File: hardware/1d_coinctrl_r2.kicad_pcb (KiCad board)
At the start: 2 copper layers, 158.8 x 159.8 mm, 97 parts, among them J1 +12V INPUT, J10 USB_B, J2 CO LINE, J3 V_RLY_SEL, J5 COIN LINE, J6 DB9_Female_MountingHoles, J7 Conn_01x02, J8 Conn_02x10_Odd_Even, J9 Conn_01x06_Male, K1 G5V-2-DC12, K10 L4_COIN_CTRL, K11 G5V-2-DC12, K2 G5V-2-DC12, K3 L1_HOLD, K4 L1_COIN_CTRL, K5 L2_HOLD, K6 L2_COIN_CTRL, K7 L3_HOLD, K8 L3_COIN_CTRL, K9 L4_HOLD, SW1 SW_Push, U1 MCP23008-xP, U10 ILD74, U14 MAX202, U2 V7805-1000, U3 PIC18F4550-IP, U4 74LS06, U5 74LS06, U6 H11AA1, U7 ILD74, U8 ILD74, U9 ILD74

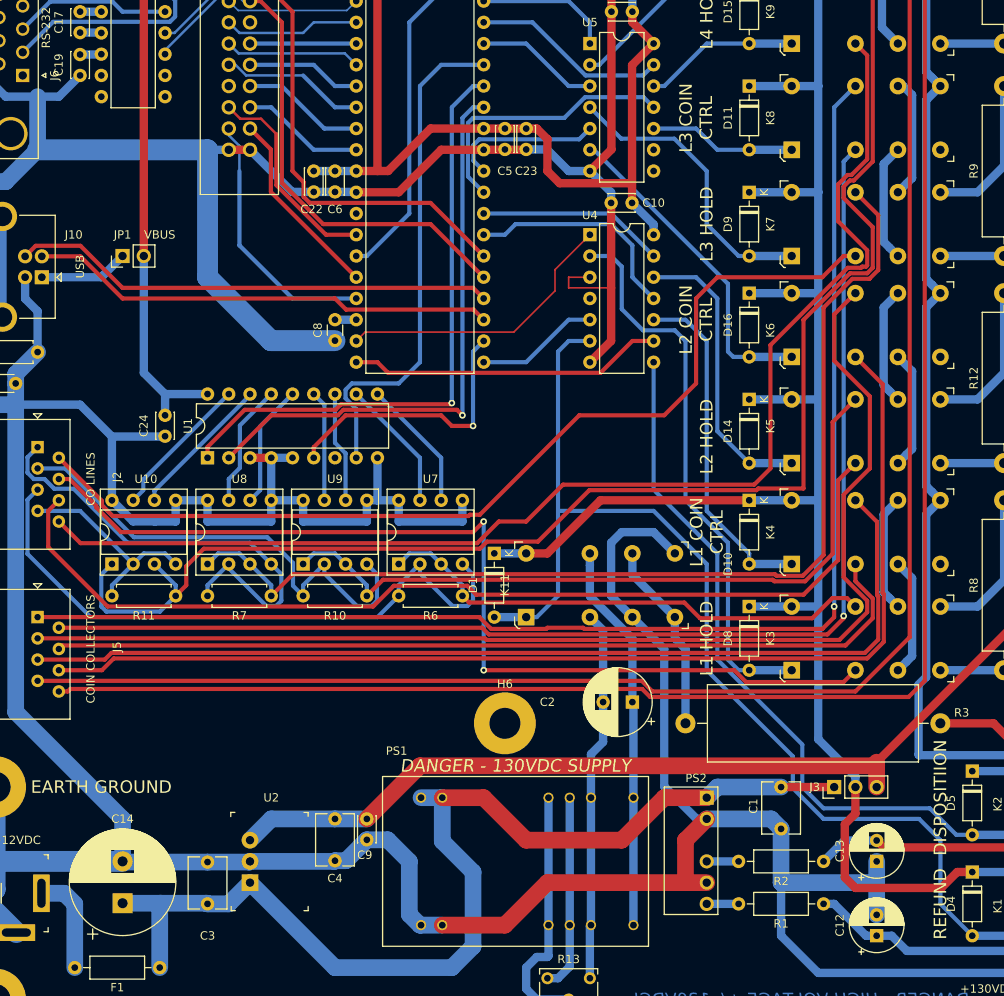
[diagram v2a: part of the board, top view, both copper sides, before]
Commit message: Resolve Issue #1: typographical error on board
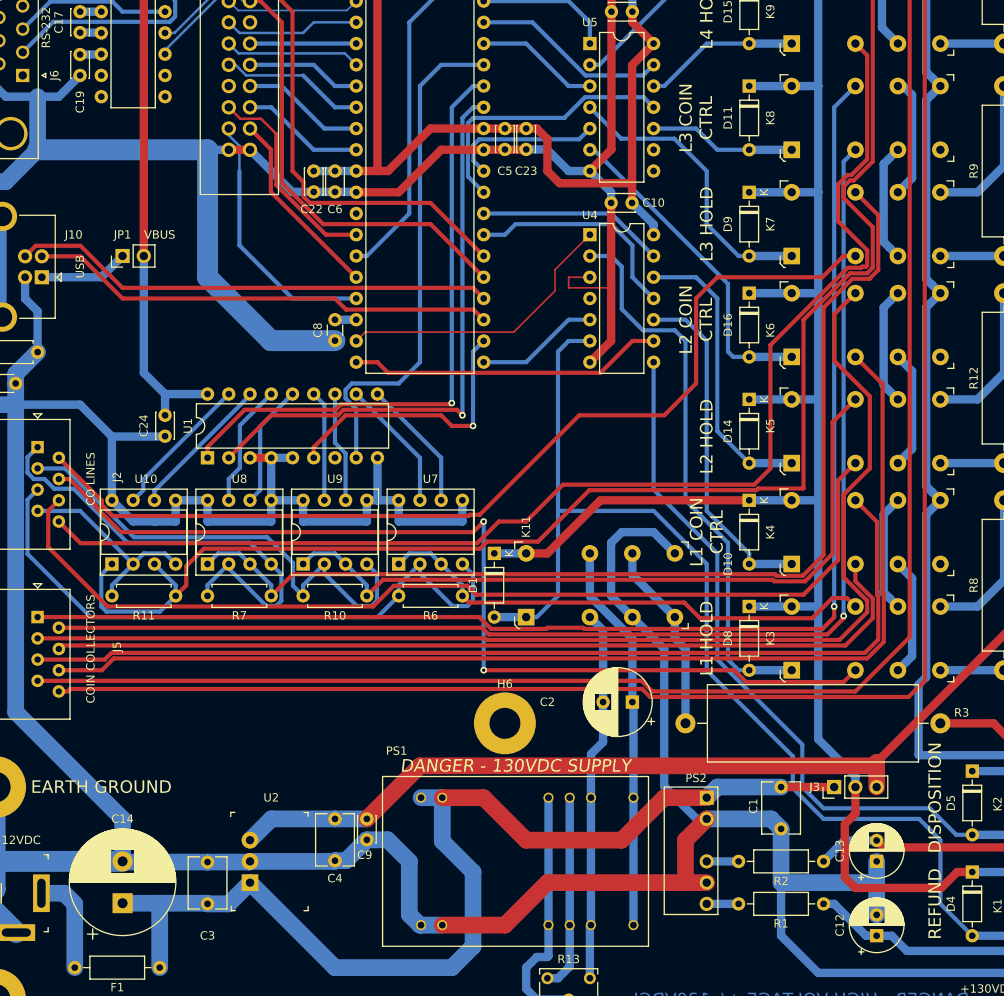
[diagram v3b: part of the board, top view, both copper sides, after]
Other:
- rule pad_to_mask_clearance: 0.051 -> 0
- board text added: "DISPOSITION"
- board text removed: "DISPOSITIION"
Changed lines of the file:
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@@
   )
   (setup
-    (pad_to_mask_clearance 0.051)
-    (solder_mask_min_width 0.25)
+    (stackup
+      (layer "F.SilkS" (type "Top Silk Screen"))
+      (layer "F.Paste" (type "Top Solder Paste"))
+      (layer "F.Mask" (type "Top Solder Mask") (thickness 0.01))
+      (layer "F.Cu" (type "copper") (thickness 0.035))
+      (layer "dielectric 1" (type "core") (thickness 1.51) (material "FR4") (epsilon_r 4.5) (loss_tangent 0.02))
+      (layer "B.Cu" (type "copper") (thickness 0.035))
+      (layer "B.Mask" (type "Bottom Solder Mask") (thickness 0.01))
+      (layer "B.Paste" (type "Bottom Solder Paste"))
+      (layer "B.SilkS" (type "Bottom Silk Screen"))
+      (copper_finish "None")
+      (dielectric_constraints no)
+    )
+    (pad_to_mask_clearance 0)
     (pcbplotparams
       (layerselection 0x00010fc_ffffffff)
@@
     (property "Status" "Active")
     (attr through_hole)
-    (fp_text reference "K11" (at -2.54 -3.81 90) (layer "F.SilkS")
+    (fp_text reference "K11" (at 0 -10.795 90) (layer "F.SilkS")
       (effects (font (size 1 1) (thickness 0.15)))
     )
@@
     (property "Sheetname" "UART")
     (attr through_hole)
-    (fp_text reference "C19" (at 1.23 2.54 90) (layer "F.SilkS")
+    (fp_text reference "C19" (at 5.675 0 90) (layer "F.SilkS")
       (effects (font (size 1 1) (thickness 0.15)))
     )
@@
     (effects (font (size 1.5 1.5) (thickness 0.3)))
   )
-  (gr_text "DISPOSITIION" (at 204.47 146.05 90) (layer "F.SilkS")
+  (gr_text "DISPOSITION" (at 203.835 146.05 90) (layer "F.SilkS")
     (effects (font (size 1.5 1.5) (thickness 0.3)))
   )
@@
     (effects (font (size 1 1) (thickness 0.15)))
   )
-  (gr_text "REFUND\n" (at 204.47 158.75 90) (layer "F.SilkS")
+  (gr_text "REFUND\n" (at 203.835 158.75 90) (layer "F.SilkS")
     (effects (font (size 1.5 1.5) (thickness 0.3)))
   )

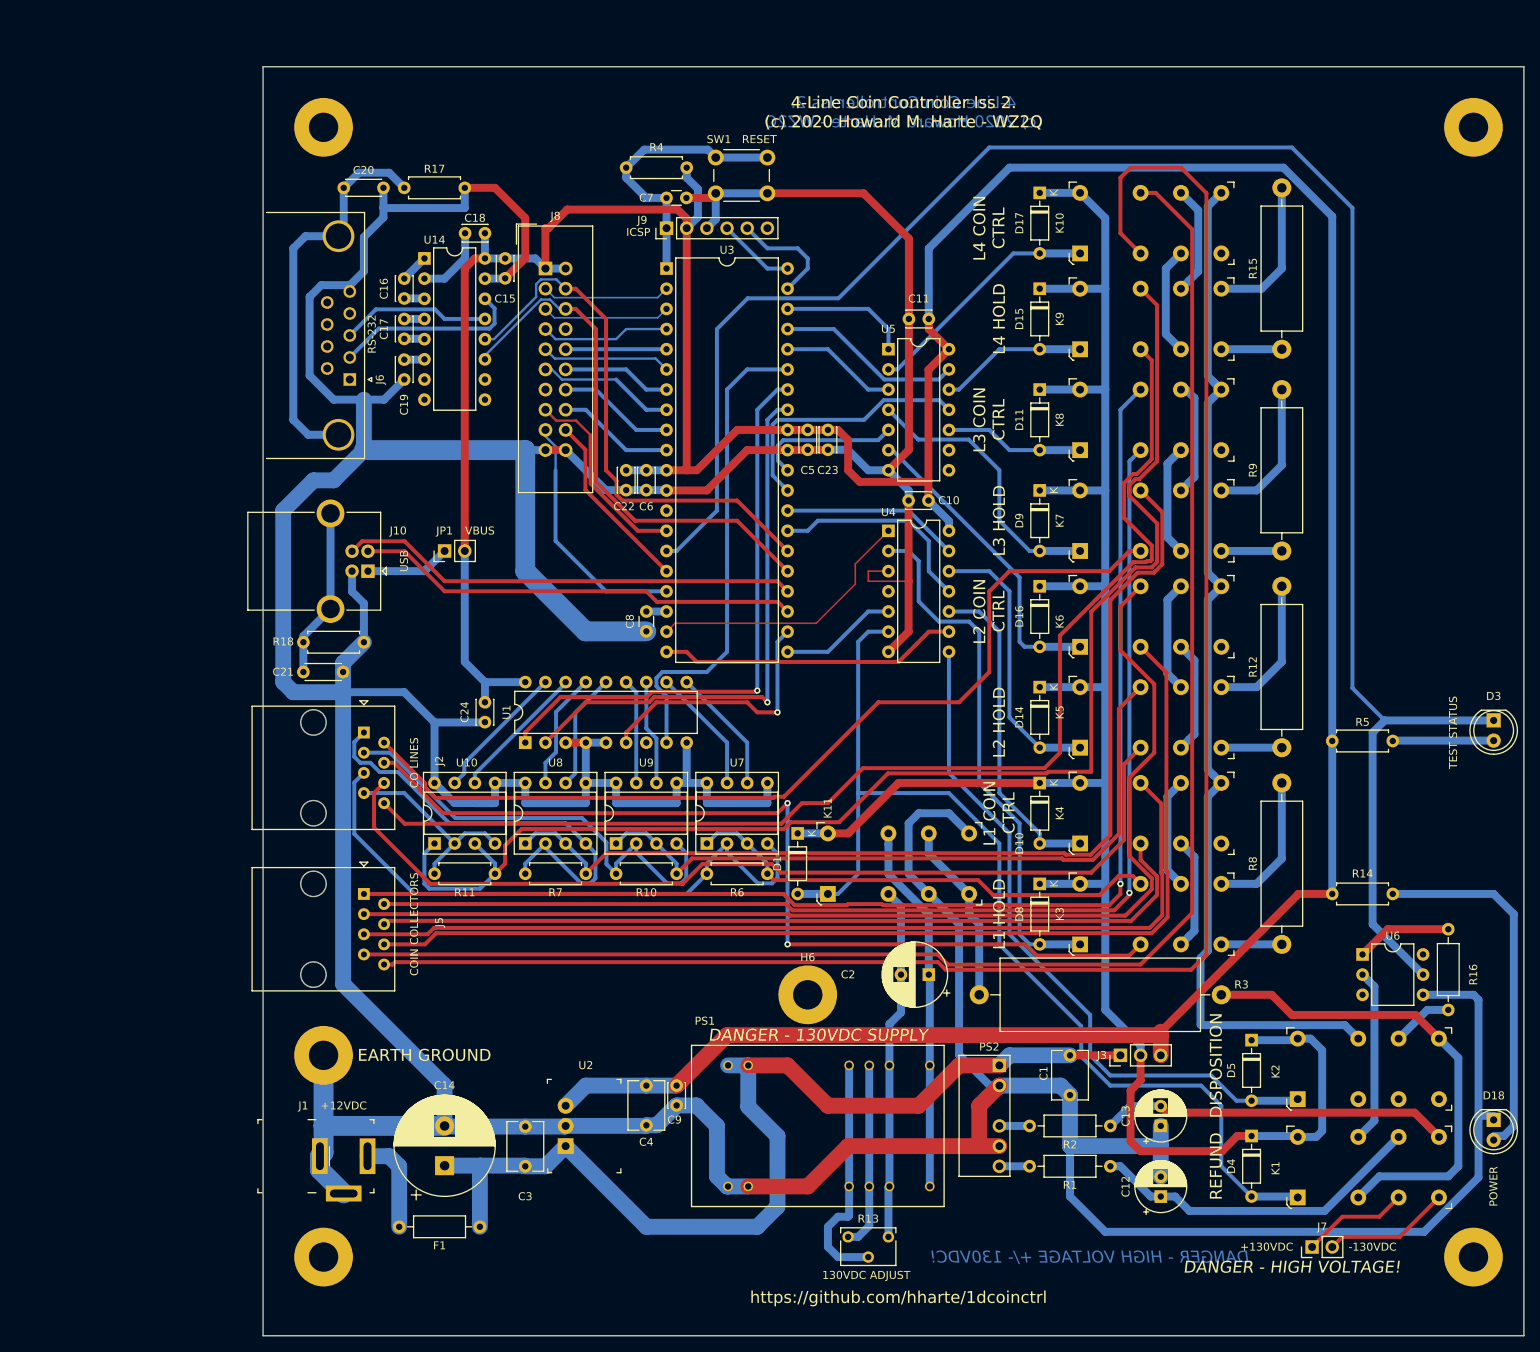
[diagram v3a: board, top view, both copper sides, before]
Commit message: Issue 3:
* Remove barrel jack, replace with 4-position terminal block with
  provision for +/- 130VDC input in case the user already has an
  appropriate power supply and does not want the on-board
  DC-DC converter.  Note: 130V DC-DC converter PS2, relay
  K8, C14, D10, and R16 must be omitted during assembly.
* Add bi-color LEDs for line status.
  Green=Off-hook, normal polarity.
  Red=Off-hook, reverse polarity.
  Off=on-hook.
* Add header for FTDI USB UART, if user does not RS-232 UART levels.
  To use the FTDI header, do not populate U1 and other components on
  pp. 3 of the schematic.
* Remove i2c I/O expander and use PIC GPIOs directly.
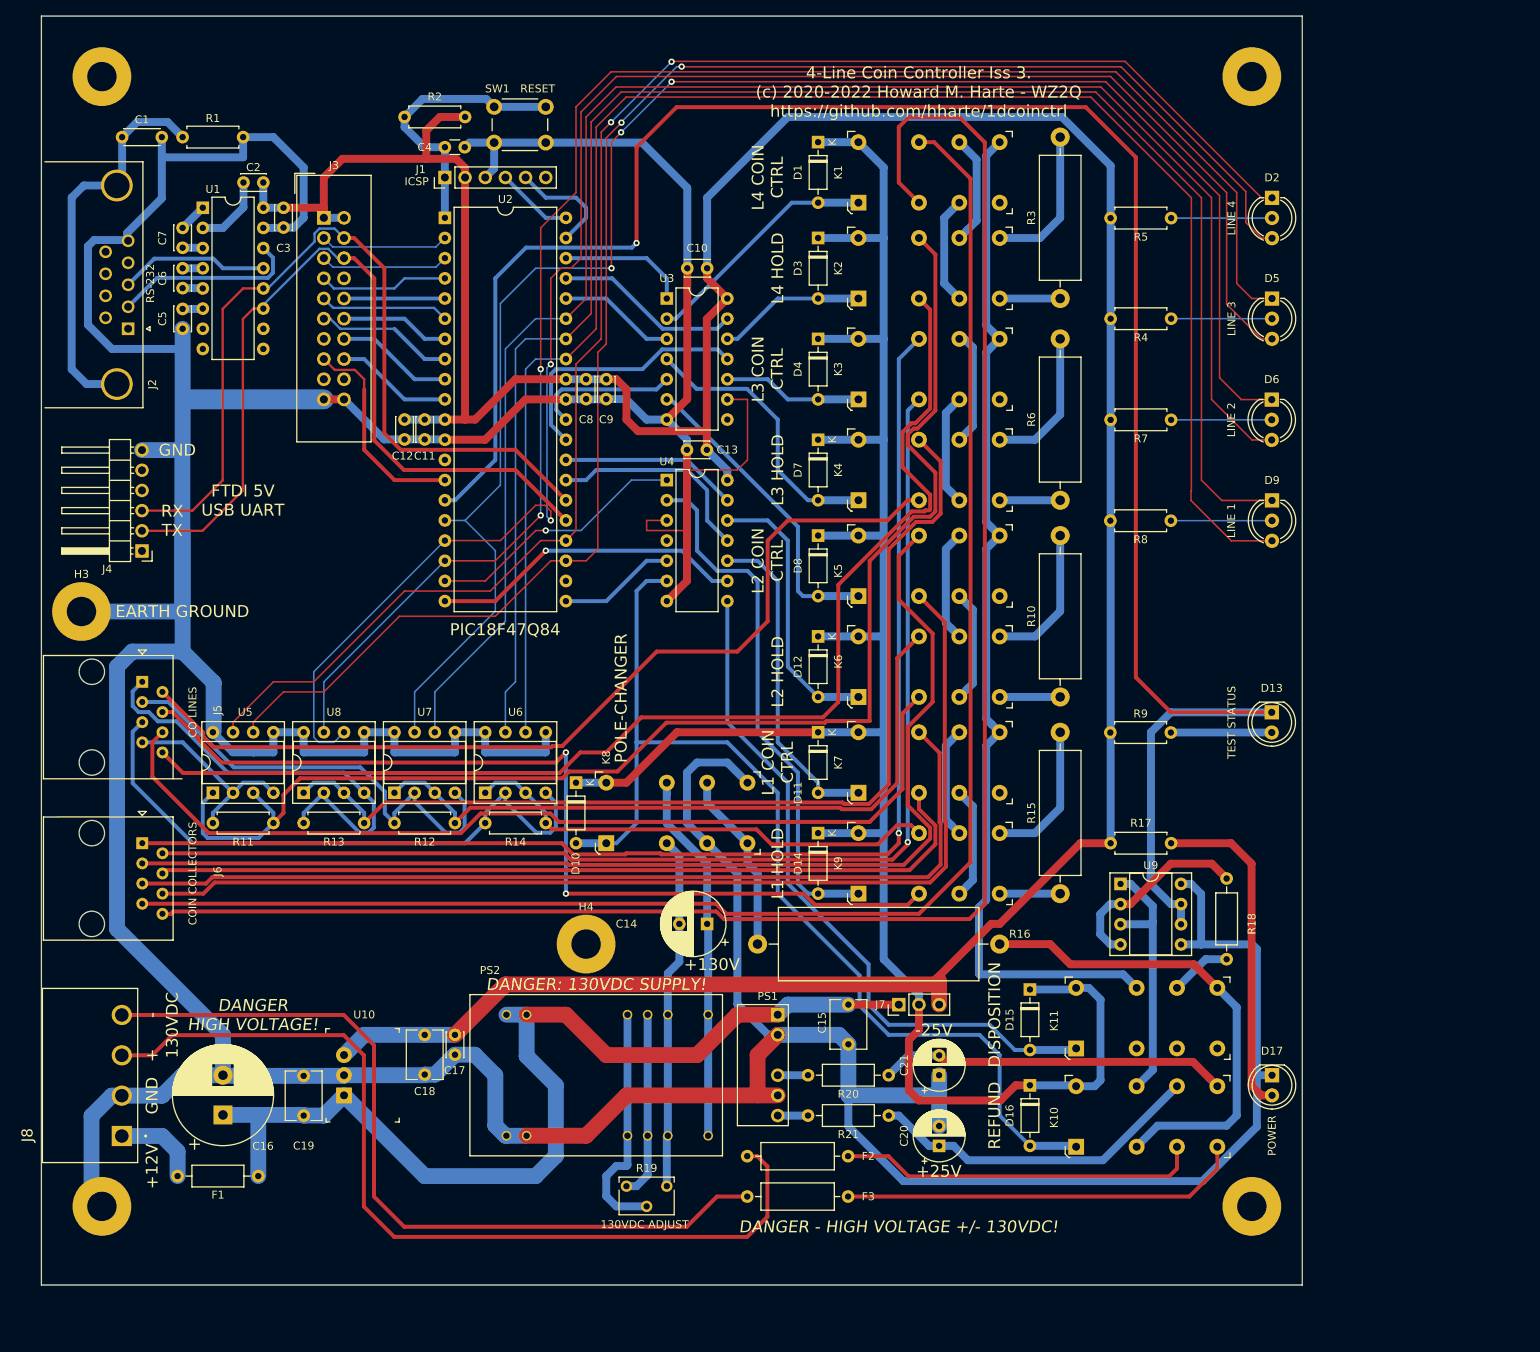
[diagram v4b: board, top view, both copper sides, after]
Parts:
- removed the C21 at (88.9, 96.5)
- removed C24: 0.1uF, Capacitor_THT:C_Disc_D3.0mm_W2.0mm_P2.50mm
- removed the C8 at (132.1, 91.4)
- removed the H1 at (91.4, 170.2)
- removed the J1 at (94.0, 157.5)
- removed J10: USB_B, Connector_USB:USB_B_OST_USB-B1HSxx_Horizontal
- removed the J7 at (215.9, 168.9)
- removed JP1: Jumper_2_Open, Connector_PinHeader_2.54mm:PinHeader_1x02_P2.54mm_Vertical
- removed the R18 at (88.9, 92.8)
- removed the U1 at (116.8, 105.4)
- removed the U6 at (222.2, 132.1)
- added D2: LED_Dual_KAK, LED_THT:LED_D5.0mm-3, F.Cu at (210.9, 36.8)
- added D5: LED_Dual_KAK, LED_THT:LED_D5.0mm-3, F.Cu at (210.9, 49.5)
- added D6: LED_Dual_KAK, LED_THT:LED_D5.0mm-3, F.Cu at (210.8, 62.2)
- added D9: LED_Dual_KAK, LED_THT:LED_D5.0mm-3, F.Cu at (210.9, 74.9)
- added F2: Fuse 100mA, Resistor_THT:R_Axial_DIN0309_L9.0mm_D3.2mm_P12.70mm_Horizontal, F.Cu at (157.5, 157.5)
- added F3: Fuse 100mA, Resistor_THT:R_Axial_DIN0309_L9.0mm_D3.2mm_P12.70mm_Horizontal, F.Cu at (157.5, 162.6)
- added H3: MountingHole_Pad, MountingHole:MountingHole_3.7mm_Pad, F.Cu at (61.0, 88.9)
- added J4: Conn_01x06_Male, Connector_PinHeader_2.54mm:PinHeader_1x06_P2.54mm_Horizontal, F.Cu at (68.6, 81.3)
- added J8: TBP01R1-508-04BE, hardware:CUI_TBP01R1-508-04BE, F.Cu at (66.0, 154.9)
- added R4: 220, Resistor_THT:R_Axial_DIN0207_L6.3mm_D2.5mm_P7.62mm_Horizontal, F.Cu at (198.2, 52.0)
- added R5: 220, Resistor_THT:R_Axial_DIN0207_L6.3mm_D2.5mm_P7.62mm_Horizontal, F.Cu at (198.2, 39.4)
- added R7: 220, Resistor_THT:R_Axial_DIN0207_L6.3mm_D2.5mm_P7.62mm_Horizontal, F.Cu at (198.2, 64.8)
- added R8: 220, Resistor_THT:R_Axial_DIN0207_L6.3mm_D2.5mm_P7.62mm_Horizontal, F.Cu at (198.1, 77.5)
- added U9: ILD74, Package_DIP:DIP-8_W7.62mm_Socket, F.Cu at (191.8, 123.2)
- U2: renamed from U3; value PIC18F4550-IP -> PIC18F47Q84-IP
- moved H5 33.8 mm to (63.5, 163.8)
- moved D1 28.6 mm to (153.7, 29.8)
- moved D11 28.6 mm to (153.7, 104.1)
- moved D12 28.6 mm to (153.7, 92.0)
- moved D14 28.6 mm to (153.7, 116.8)
- moved D3 28.6 mm to (153.7, 41.9)
- moved D4 28.6 mm to (153.7, 54.6)
- moved D7 28.6 mm to (153.7, 67.3)
- moved D8 28.6 mm to (153.7, 79.3)
- moved C11 28.6 mm to (104.2, 64.7)
- moved C16 28.6 mm to (78.8, 152.3)
- moved C18 28.6 mm to (104.2, 142.2)
- moved U7 28.6 mm to (100.4, 111.7)
- moved K10 28.6 mm to (186.2, 156.3)
- moved K11 28.6 mm to (186.2, 143.9)
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- renumbered C20 to C1, C11 to C10, C6 to C11, C22 to C12, C10 to C13, C2 to C14, C1 to C15, C14 to C16, C9 to C17, C4 to C18, C3 to C19, C18 to C2, C12 to C20, C13 to C21, C15 to C3, C7 to C4, C19 to C5, C17 to C6, C16 to C7, C5 to C8, C23 to C9, D17 to D1, D1 to D10, D10 to D11, D14 to D12, D3 to D13, D8 to D14, D5 to D15, D4 to D16, D18 to D17, D15 to D3, D11 to D4, D9 to D7, D16 to D8, H3 to H1, H4 to H2, H6 to H4, H2 to H6, J9 to J1, J6 to J2, J8 to J3, J2 to J5, J5 to J6, J3 to J7, K10 to K1, K1 to K10, K2 to K11, K9 to K2, K8 to K3, K7 to K4, K6 to K5, K5 to K6, K4 to K7, K11 to K8, K3 to K9, PS2 to PS1, PS1 to PS2, R17 to R1, R12 to R10, R10 to R12, R7 to R13, R6 to R14, R8 to R15, R3 to R16, R14 to R17, R16 to R18, R13 to R19, R4 to R2, R2 to R20, R1 to R21, R15 to R3, R9 to R6, R5 to R9, U14 to U1, U2 to U10, U5 to U3, U10 to U5, U7 to U6, U9 to U7
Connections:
- F1 pad 2: Net-(F1-Pad2) -> /12VIN
- U2 pad 16: /GPIO/CCP2 -> /GPIO/L2_OFF_HOOK_R
- U2 pad 17: /GPIO/CCP1 -> /GPIO/L3_OFF_HOOK_F
- U2 pad 18: Net-(C8-Pad2) -> /GPIO/L3_OFF_HOOK_R
- U2 pad 22: /GPIO/I2C_RESET -> unconnected-(U2-Pad22)
- U2 pad 23: /GPIO/USB_DM -> /GPIO/L4_OFF_HOOK_F
- U2 pad 24: /GPIO/USB_DP -> /GPIO/L4_OFF_HOOK_R
- U2 pad 33: /GPIO/I2C_SDA -> /Coin Line Control/L1_OFF_HOOK_F
- U2 pad 34: /GPIO/I2C_SCL -> /Coin Line Control/L1_OFF_HOOK_R
- U2 pad 35: /GPIO/I2C_INT -> /Coin Line Control/L2_OFF_HOOK_F
- U3 pad 8: (no net) -> unconnected-(U3-Pad8)
- U3 pad 9: (no net) -> GND
- U5 pad 6: /Coin Line Control/L4_OFF_HOOK_F -> /GPIO/L4_OFF_HOOK_F
- U5 pad 7: /Coin Line Control/L4_OFF_HOOK_R -> /GPIO/L4_OFF_HOOK_R
- U7 pad 7: /Coin Line Control/L2_OFF_HOOK_R -> /GPIO/L2_OFF_HOOK_R
- U8 pad 6: /Coin Line Control/L3_OFF_HOOK_F -> /GPIO/L3_OFF_HOOK_F
- U8 pad 7: /Coin Line Control/L3_OFF_HOOK_R -> /GPIO/L3_OFF_HOOK_R
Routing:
- net /GPIO/L3_OFF_HOOK_F: track 0.00 -> 217.8 mm, vias 0 -> 2
- net /GPIO/L2_OFF_HOOK_R: track 0.00 -> 212.2 mm, vias 0 -> 3
- net /GPIO/L4_OFF_HOOK_F: track 0.00 -> 204.7 mm, vias 0 -> 2
- net /GPIO/L3_OFF_HOOK_R: track 0.00 -> 203.6 mm, vias 0 -> 2
- net /GPIO/L4_OFF_HOOK_R: track 0.00 -> 201.2 mm, vias 0 -> 2
- net /Coin Line Control/L1_OFF_HOOK_F: track 15.9 -> 214.3 mm
- net /Coin Line Control/L1_OFF_HOOK_R: track 15.9 -> 213.7 mm
- net /Coin Line Control/L2_OFF_HOOK_F: track 13.2 -> 208.8 mm
- net Net-(F2-Pad2): track 0.00 -> 114.5 mm
- net Net-(F3-Pad2): track 0.00 -> 102.5 mm
- net /GPIO/I2C_SCL: track 72.9 -> 0.00 mm, vias 1 -> 0
- net /GPIO/I2C_SDA: track 69.2 -> 0.00 mm, vias 1 -> 0
- net +5V: track 480.0 -> 417.6 mm
- net /GPIO/I2C_INT: track 60.6 -> 0.00 mm
- net /GPIO/USB_DP: track 58.0 -> 0.00 mm
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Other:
- board text added: "+"
- board text added: "+12V"
- board text added: "+130V"
- board text added: "+25V"
- board text added: "-"
- board text added: "-25V"
- board text added: "130VDC"
- board text added: "4-Line Coin Controller Iss 3. (c) 2020-2022 Howard M. Harte - WZ2Q https://github.com/hharte/1dcoinctrl"
- board text added: "DANGER HIGH VOLTAGE!"
- board text added: "DANGER: 130VDC SUPPLY!"
- board text added: "FTDI 5V USB UART"
- board text added: "GND"
- board text added: "LINE 1"
- board text added: "LINE 2"
- board text added: "LINE 3"
- board text added: "LINE 4"
- board text added: "PIC18F47Q84"
- board text added: "POLE-CHANGER"
- board text added: "RX TX"
- board text removed: "+12VDC"
- board text removed: "4-Line Coin Controller Iss 2. (c) 2020 Howard M. Harte - WZ2Q"
- board text removed: "DANGER - 130VDC SUPPLY"
- board text removed: "DANGER - HIGH VOLTAGE!"
- board text removed: "USB"
- board text removed: "VBUS"
- board text removed: "https://github.com/hharte/1dcoinctrl"
